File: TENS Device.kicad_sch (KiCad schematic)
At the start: 11 parts

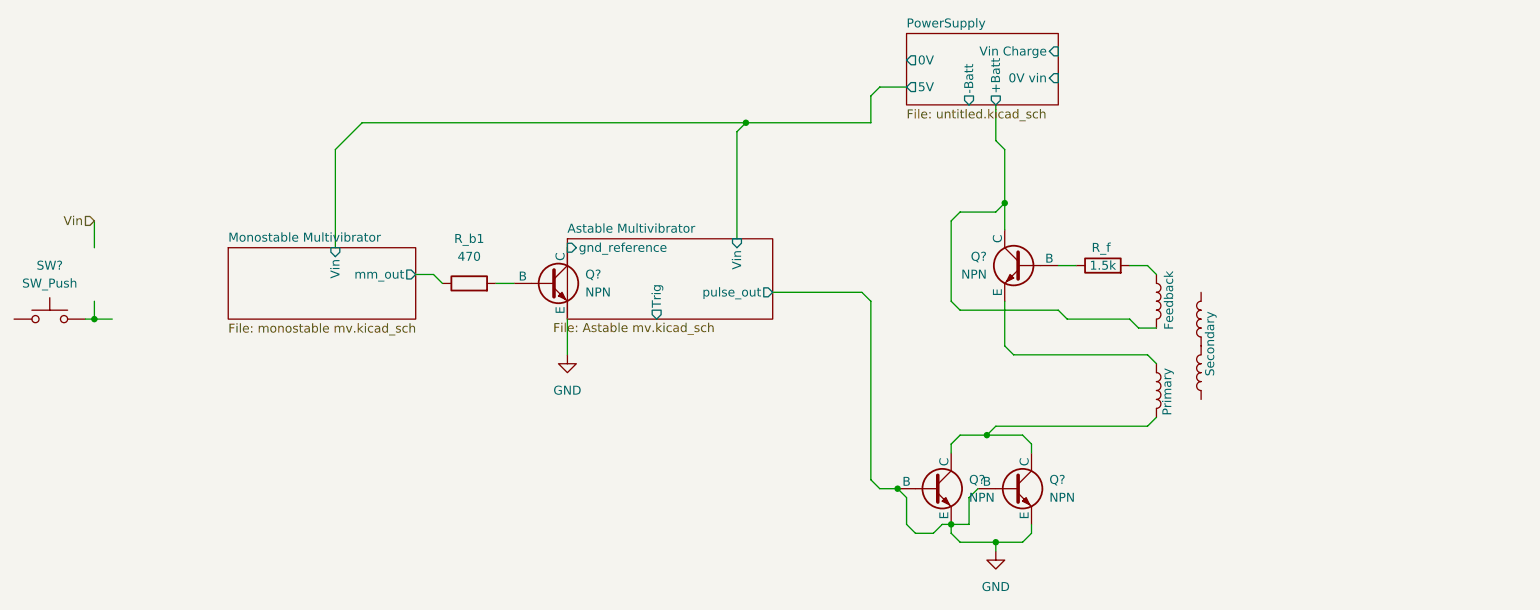
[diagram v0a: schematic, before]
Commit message: added Multipage Schematics
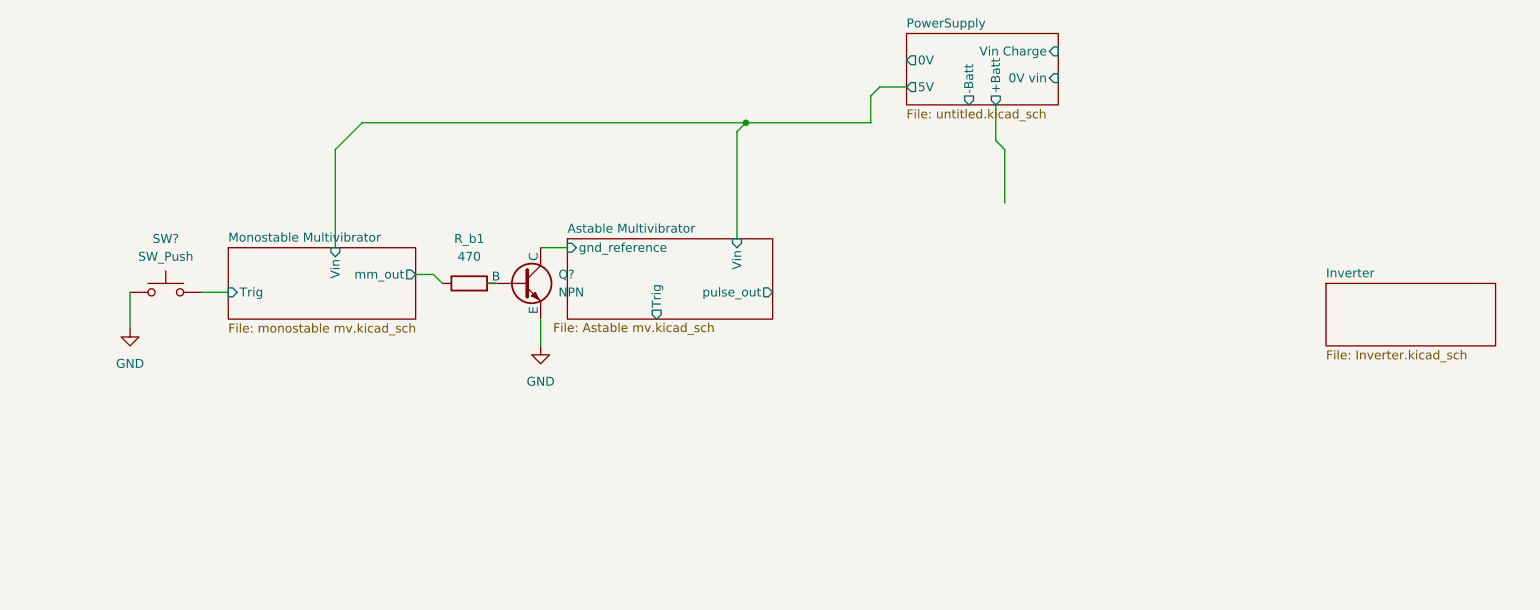
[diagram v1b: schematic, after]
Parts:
- removed Feedback, L?, Primary, Secondary: L, symbol Device:L
- removed Q? (x3): NPN, symbol Simulation_SPICE:NPN
- removed R_f: 1.5k, symbol Device:R
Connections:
- net GND: now also SW?.1
- net Monostable Multivibrator/Trig: now reaches SW?.2
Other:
- added sheet Inverter (Inverter.kicad_sch)
- sheet Monostable Multivibrator ports: added Trig; removed none
- moved on the sheet: Q?, SW?
